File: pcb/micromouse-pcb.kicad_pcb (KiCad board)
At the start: 4 copper layers, 126.2 x 95 mm, 65 parts, among them J1 Conn_01x08, J1_MotorEncoder1 Conn_01x06, J2_MotorEncoder1 Conn_01x06, J3 Conn_01x08, J4 Conn_01x08, Q1 BS170, Q2 TEFT4300, Q3 BS170, Q4 TEFT4300, Q5 BS170, Q6 TEFT4300, Q7 BS170, Q8 TEFT4300, Q9 FQP27P06, SW2 SW_SPDT, U1 Teensy_4.1, U2 L7805

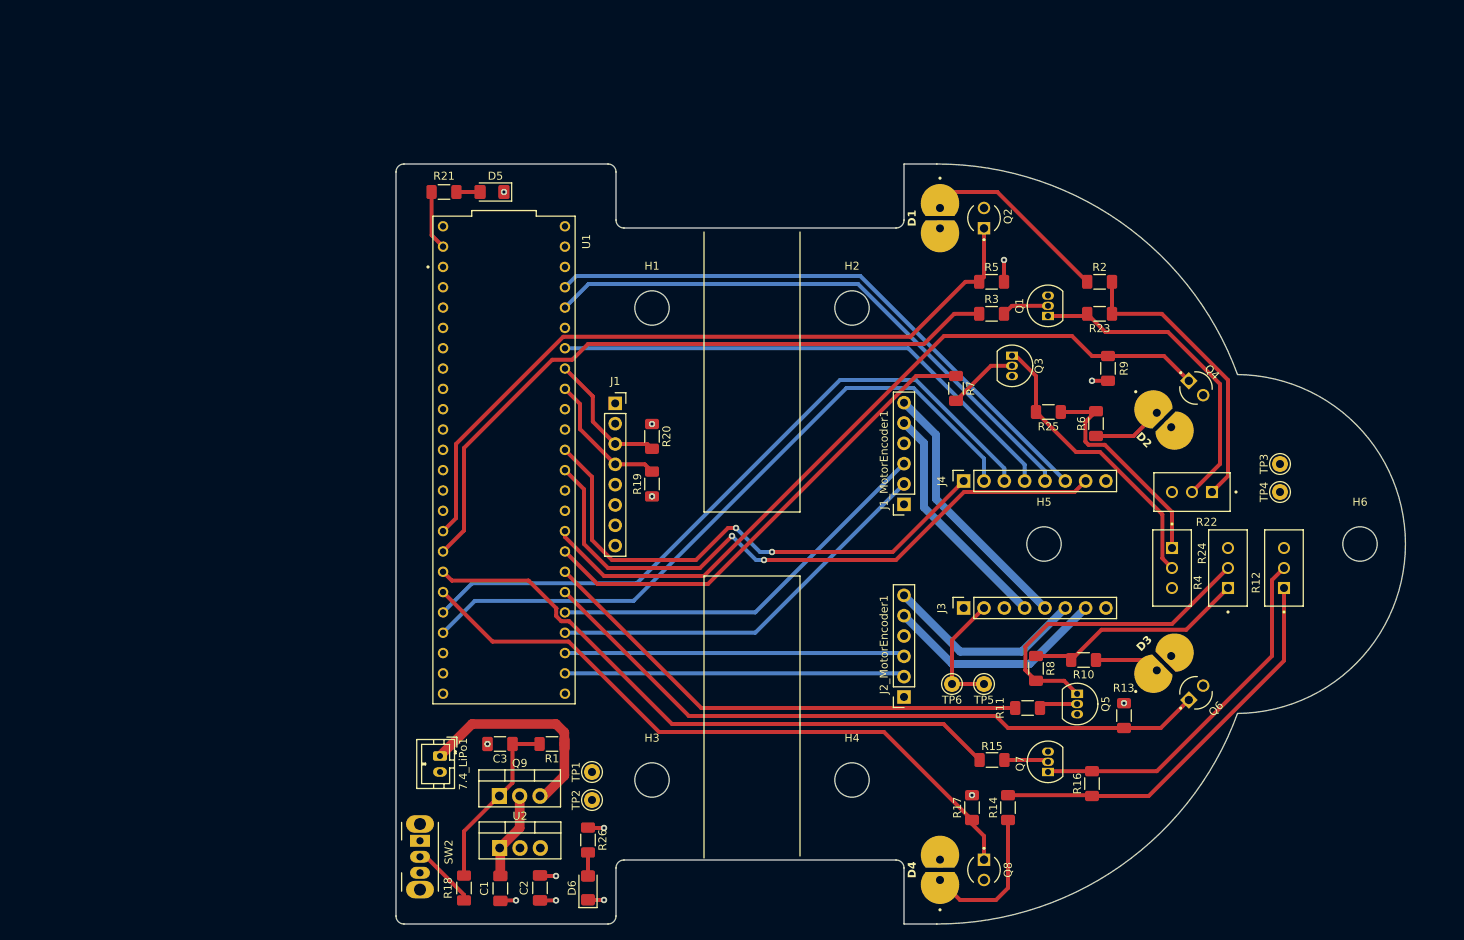
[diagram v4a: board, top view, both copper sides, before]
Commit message: updated pcb with buttons
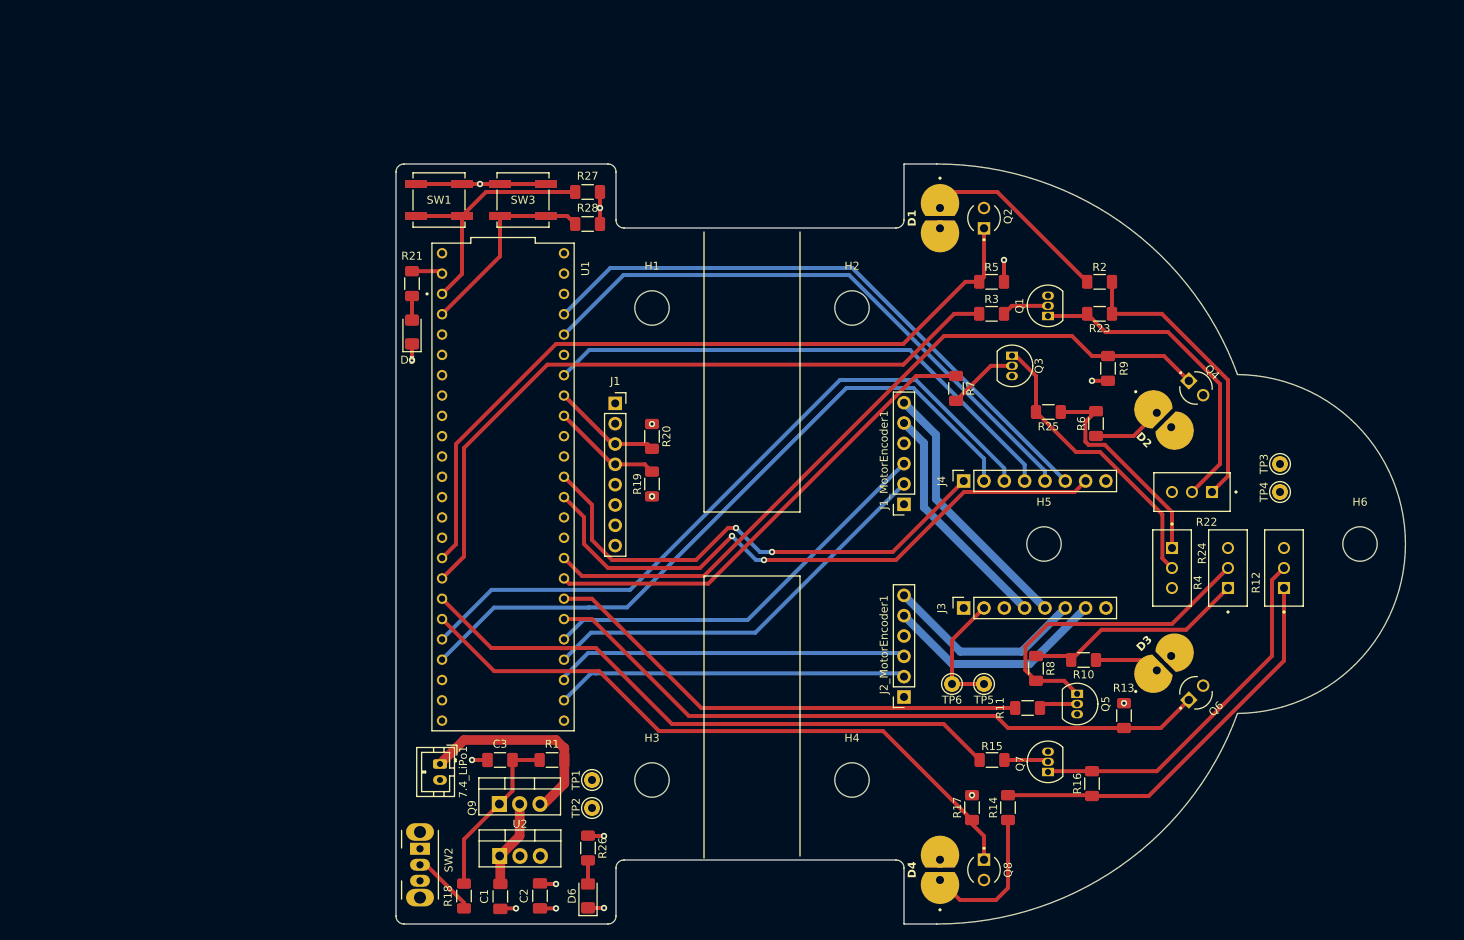
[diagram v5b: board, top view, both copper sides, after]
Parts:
- added R27: 10k, Resistor_SMD:R_1206_3216Metric_Pad1.30x1.75mm_HandSolder, F.Cu at (51.0, 21.0)
- added R28: 10k, Resistor_SMD:R_1206_3216Metric_Pad1.30x1.75mm_HandSolder, F.Cu at (51.0, 25.0)
- added SW1: SW_Push, Button_Switch_SMD:SW_SPST_B3SL-1002P, F.Cu at (32.4, 22.0)
- added SW3: SW_Push, Button_Switch_SMD:SW_SPST_B3SL-1002P, F.Cu at (42.9, 22.0)
- moved D5 20.2 mm to (29.0, 38.5), turned to 90 degrees
- moved R21 12.1 mm to (29.0, 32.5), turned to 90 degrees
- moved U1 3.37 mm to (40.4, 57.9)
- moved C3 2.00 mm to (40.0, 92.0)
- moved R1 2.00 mm to (46.5, 92.0)
- moved 7.4_LiPo1 1.00 mm to (32.5, 92.5)
- moved C1 1.00 mm to (40.0, 109.0)
- moved C2 1.00 mm to (45.0, 109.0)
- moved D6 1.00 mm to (51.0, 109.0)
- moved Q9 1.00 mm to (39.9, 97.5)
- moved R18 1.00 mm to (35.5, 109.0)
- moved R26 1.00 mm to (51.0, 103.0)
- moved SW2 1.00 mm to (30.0, 103.1)
- moved TP1 1.00 mm to (51.5, 94.5)
- moved TP2 1.00 mm to (51.5, 98.0)
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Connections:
- U1 pad 1: unconnected-(U1-TX1-Pad1) -> Net-(U1-TX1)
- U1 pad 2: unconnected-(U1-OUT2-Pad2) -> Net-(U1-OUT2)
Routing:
- net Net-(U1-TX1): track 0.00 -> 31.9 mm
- net Net-(U1-OUT2): track 0.00 -> 25.1 mm
- net GND: track 10.7 -> 30.9 mm, vias 9 -> 10
- net +3.3V: track 0.00 -> 4.00 mm, vias 2 -> 3
- net Net-(U1-RX1): track 7.42 -> 3.88 mm
- net Receiver 1: track 92.3 -> 95.7 mm
- net Emitter 1: track 85.4 -> 88.8 mm
- net PWMA_6612: track 66.7 -> 63.4 mm
- net PWMB_6612: track 81.1 -> 77.8 mm
- net SCL: track 16.9 -> 13.8 mm
- net SDA: track 17.0 -> 13.9 mm
- net PWM M2_A: track 72.2 -> 74.6 mm
- net PWM M2_B: track 73.7 -> 76.1 mm
- net Emitter 4: track 77.5 -> 75.6 mm
- net ENC_M2_B: track 42.5 -> 44.3 mm
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
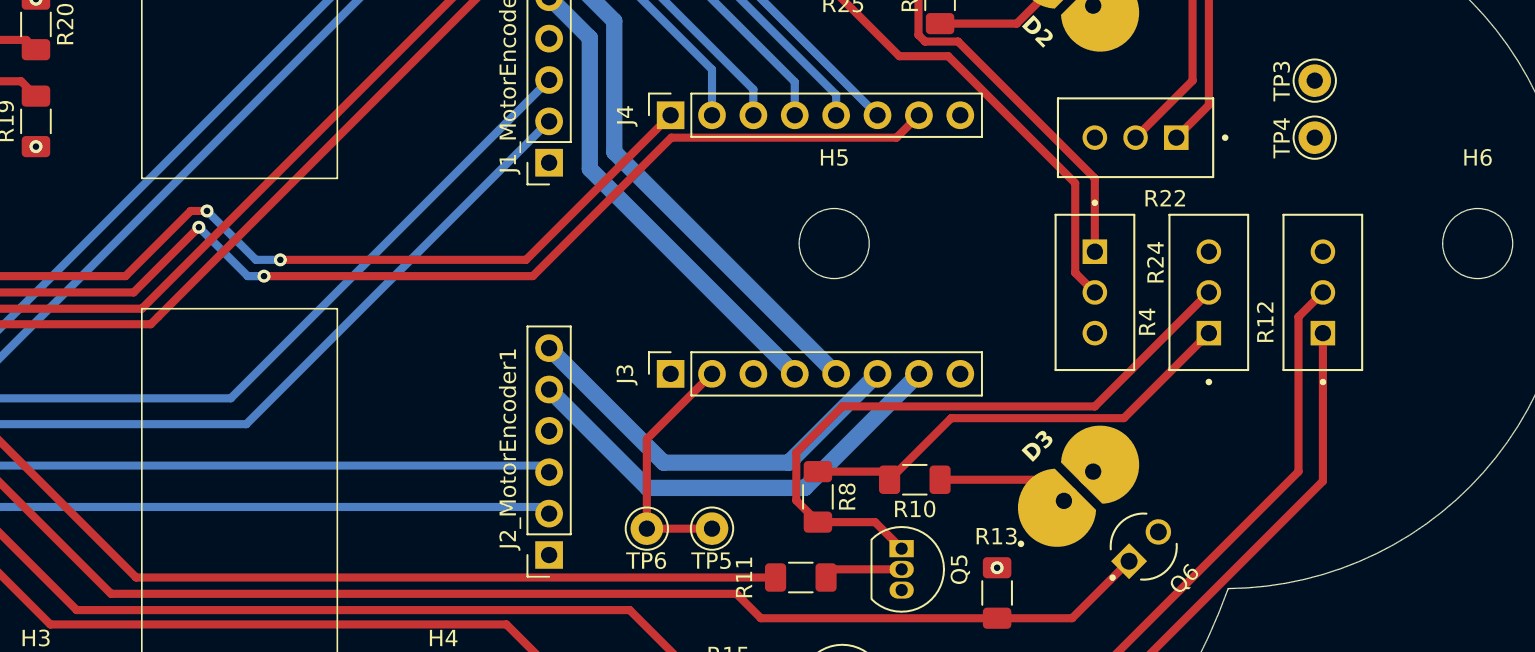
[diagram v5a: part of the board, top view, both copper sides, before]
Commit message: Added robobuzz
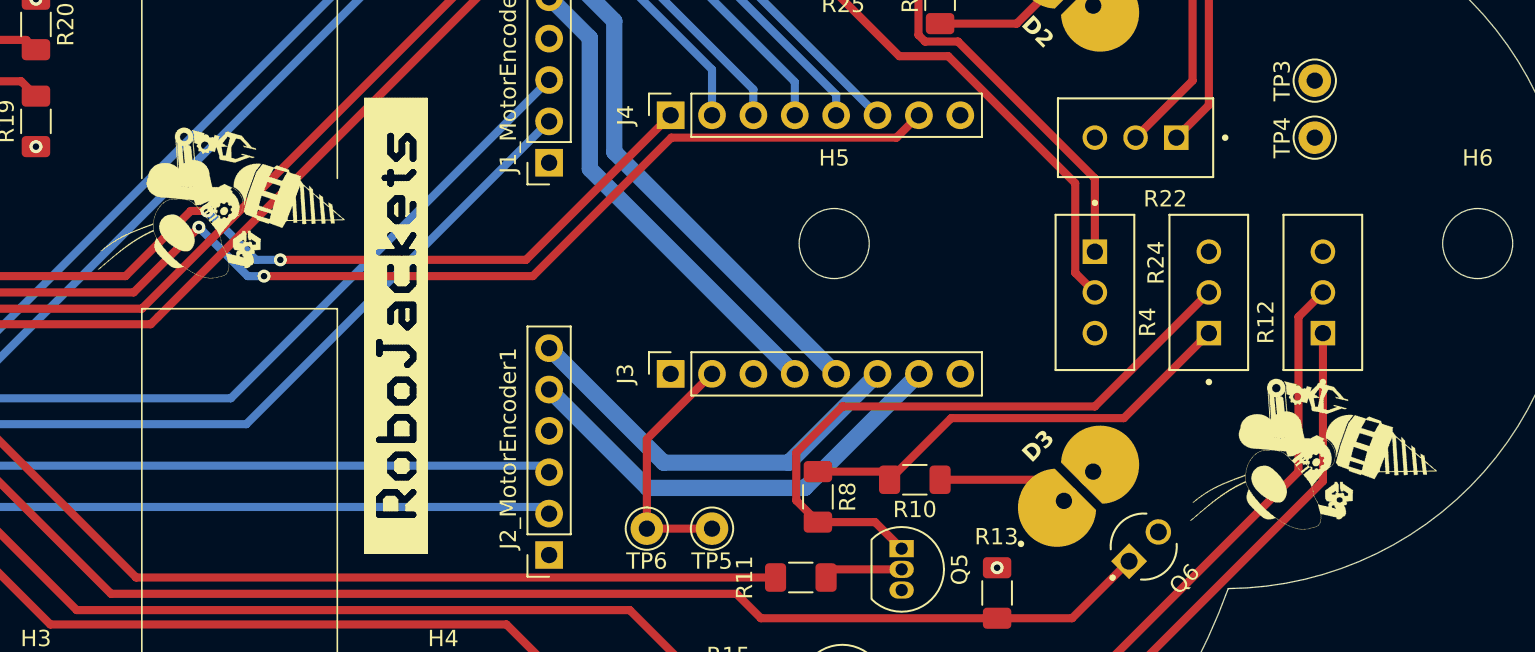
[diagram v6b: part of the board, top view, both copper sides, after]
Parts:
- added ?: , micromouse:ROBOJACKETS, F.Cu at (83.0, 84.0)
- added ?: , micromouse:ROBOBUZZ_0.8X, F.Cu at (78.0, 63.6)
- added ?: , micromouse:ROBOBUZZ_0.8X, F.Cu at (145.0, 79.0)

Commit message: Added Ratatoulli name
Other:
- board text added: "Ratatouilli"
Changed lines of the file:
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@@
 		(layer "Edge.Cuts")
+	)
+	(gr_text "Ratatouilli"
+		(at 144 66.5 90)
+		(layer "F.SilkS")
+		(effects
+			(font
+				(size 2 2)
+				(thickness 0.3)
+				(bold yes)
+			)
+			(justify left bottom)
+		)
 	)
 	(dimension
